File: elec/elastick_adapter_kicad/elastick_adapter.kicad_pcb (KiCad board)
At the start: 2 copper layers, 12 parts, among them J2 DE9_Pins_MountingHoles

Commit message: update kicad
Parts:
- removed R12, R13, R14, R16, R17, R25, R26, R27, R4: 330, Resistor_THT:R_Axial_DIN0207_L6.3mm_D2.5mm_P7.62mm_Horizontal
- added C1: 470µF, Capacitor_THT:CP_Radial_D8.0mm_P3.50mm, F.Cu at (101.3, 94.0)
- added C2: 100nF, Capacitor_THT:C_Disc_D5.0mm_W2.5mm_P5.00mm, F.Cu at (154.9, 93.9)
- added C3: 22nF, Capacitor_THT:C_Disc_D5.0mm_W2.5mm_P5.00mm, F.Cu at (97.8, 106.7)
- added C4: 22nF, Capacitor_THT:C_Disc_D5.0mm_W2.5mm_P5.00mm, F.Cu at (97.8, 115.6)
- added J2: USB-C Breakout, elastick:usbc, F.Cu at (139.0, 147.5)
- added SW1: POWER, Button_Switch_THT:SW_Slide_SPDT_Angled_CK_OS102011MA1Q, F.Cu at (106.1, 126.3)
- added SW2: ROTARY_SWITCH, Rotary_Encoder:RotaryEncoder_Alps_EC11E-Switch_Vertical_H20mm, B.Cu at (171.4, 124.5)
- DS1: renamed from U2; value ~ -> SSD1306 I2C OLED
- J1: renamed from J2; value DE9_Pins_MountingHoles -> DE-9JOYSTICK
- U1: value ~ -> LOLIN-D32
- moved DS1 72.9 mm to (127.7, 138.2), turned to 0 degrees
- moved U1 16.2 mm to (134.7, 134.8)
- moved J1 9.65 mm to (144.0, 48.6)
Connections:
- DS1 pad 1: unconnected-(U2-vcc-Pad1) -> Net-(DS1-vcc)
- DS1 pad 2: unconnected-(U2-gnd-Pad2) -> Net-(DS1-gnd)
- DS1 pad 3: unconnected-(U2-scl-Pad3) -> Net-(DS1-scl)
- DS1 pad 4: unconnected-(U2-sda-Pad4) -> Net-(DS1-sda)
- J1 pad 1: Net-(J2-Pad1) -> Net-(U1-4)
- J1 pad 2: Net-(J2-Pad2) -> Net-(U1-17)
- J1 pad 3: Net-(J2-Pad3) -> Net-(U1-26)
- J1 pad 4: Net-(J2-Pad4) -> Net-(U1-14)
- J1 pad 5: Net-(J2-Pad5) -> Net-(C4-Pad2)
- J1 pad 6: Net-(J2-Pad6) -> Net-(U1-16)
- J1 pad 7: Net-(J2-Pad7) -> Net-(U1-25)
- J1 pad 8: Net-(J2-Pad8) -> Net-(U1-27)
- J1 pad 9: Net-(J2-Pad9) -> Net-(C3-Pad2)
- U1 pad 1: unconnected-(U1-3v-Pad1) -> Net-(DS1-vcc)
- U1 pad 12: Net-(R12-Pad2) -> Net-(C3-Pad2)
- U1 pad 13: Net-(R13-Pad2) -> Net-(C4-Pad2)
- U1 pad 14: unconnected-(U1-enable-Pad14) -> Net-(SW1-B)
- U1 pad 17: unconnected-(U1-gnd-Pad17) -> Net-(DS1-gnd)
- U1 pad 21: unconnected-(U1-3-Pad21) -> Net-(DS1-sda)
- U1 pad 22: unconnected-(U1-21-Pad22) -> Net-(DS1-scl)
- U1 pad 32: unconnected-(U1-gnd-Pad32) -> Net-(DS1-gnd)
- U1 pad 5: unconnected-(U1-34-Pad5) -> Net-(U1-34)
- U1 pad 6: unconnected-(U1-32-Pad6) -> Net-(U1-32)
- U1 pad 7: unconnected-(U1-33-Pad7) -> Net-(U1-33)
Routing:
- net Net-(C4-Pad2): track 0.00 -> 122.2 mm
- net Net-(C3-Pad2): track 0.00 -> 116.2 mm
- net Net-(U1-27): track 0.00 -> 110.3 mm
- net Net-(U1-14): track 0.00 -> 109.7 mm
- net Net-(U1-26): track 0.00 -> 100.8 mm
- net Net-(U1-25): track 0.00 -> 100.0 mm
- net Net-(U1-4): track 0.00 -> 99.5 mm
- net Net-(U1-16): track 0.00 -> 98.7 mm
- net Net-(U1-17): track 0.00 -> 92.1 mm
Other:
- board text added: "ARNOKAID"
- board text added: "design by"

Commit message: update kicad
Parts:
- SW1: footprint Button_Switch_THT:SW_Slide_SPDT_Angled_CK_OS102011MA1Q -> elastick:SW_90degrees_3pins; moved to B.Cu
- moved C2 39.4 mm to (115.5, 94.1), turned to 180 degrees
- moved C1 28.5 mm to (114.3, 68.6), turned to 0 degrees
- moved J1 23.5 mm to (144.0, 72.1)
- moved C4 14.2 mm to (110.6, 109.2)
- moved C3 13.3 mm to (110.6, 102.9)
- moved SW2 11.4 mm to (160.0, 124.5)
- moved SW1 8.19 mm to (113.4, 130.0), turned to 90 degrees
- moved J2 3.08 mm to (135.9, 147.5)
- moved DS1 1.27 mm to (129.0, 138.2)
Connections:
- SW1 pad 1: Net-(DS1-gnd) -> unconnected-(SW1-A-Pad1)
- SW1 pad 2: Net-(SW1-B) -> Net-(DS1-gnd)
- SW1 pad 3: unconnected-(SW1-C-Pad3) -> Net-(SW1-C)
- SW2 pad A: Net-(U1-32) -> Net-(DS1-gnd)
- SW2 pad B: Net-(U1-34) -> Net-(U1-18)
- SW2 pad C: Net-(DS1-gnd) -> Net-(U1-19)
- SW2 pad S1: Net-(DS1-gnd) -> Net-(U1-5)
- SW2 pad S2: Net-(U1-33) -> Net-(DS1-gnd)
- U1 pad 14: Net-(SW1-B) -> Net-(SW1-C)
- U1 pad 19: unconnected-(U1-22-Pad19) -> Net-(DS1-scl)
- U1 pad 21: Net-(DS1-sda) -> unconnected-(U1-3-Pad21)
- U1 pad 22: Net-(DS1-scl) -> Net-(DS1-sda)
- U1 pad 23: unconnected-(U1-19-Pad23) -> Net-(U1-19)
- U1 pad 24: unconnected-(U1-18-Pad24) -> Net-(U1-18)
- U1 pad 25: unconnected-(U1-5-Pad25) -> Net-(U1-5)
- U1 pad 5: Net-(U1-34) -> unconnected-(U1-34-Pad5)
- U1 pad 6: Net-(U1-32) -> unconnected-(U1-32-Pad6)
- U1 pad 7: Net-(U1-33) -> unconnected-(U1-33-Pad7)
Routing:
- net Net-(DS1-gnd): track 0.00 -> 298.0 mm
- net Net-(DS1-vcc): track 0.00 -> 91.1 mm
- net Net-(DS1-scl): track 0.00 -> 47.1 mm
- net Net-(U1-27): track 110.3 -> 68.1 mm
- net Net-(U1-14): track 109.7 -> 68.9 mm
- net Net-(DS1-sda): track 0.00 -> 39.5 mm
- net Net-(U1-25): track 100.0 -> 60.7 mm
- net Net-(U1-26): track 100.8 -> 61.5 mm
- net Net-(U1-16): track 98.7 -> 65.1 mm
- net Net-(U1-4): track 99.5 -> 65.9 mm
- net Net-(U1-17): track 92.1 -> 58.5 mm
- net Net-(U1-19): track 0.00 -> 27.0 mm
- net Net-(U1-18): track 0.00 -> 27.0 mm
- net Net-(U1-5): track 0.00 -> 22.3 mm
- net Net-(C4-Pad2): track 122.2 -> 103.1 mm
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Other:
- board outline added: 55.9 x 99.1 mm

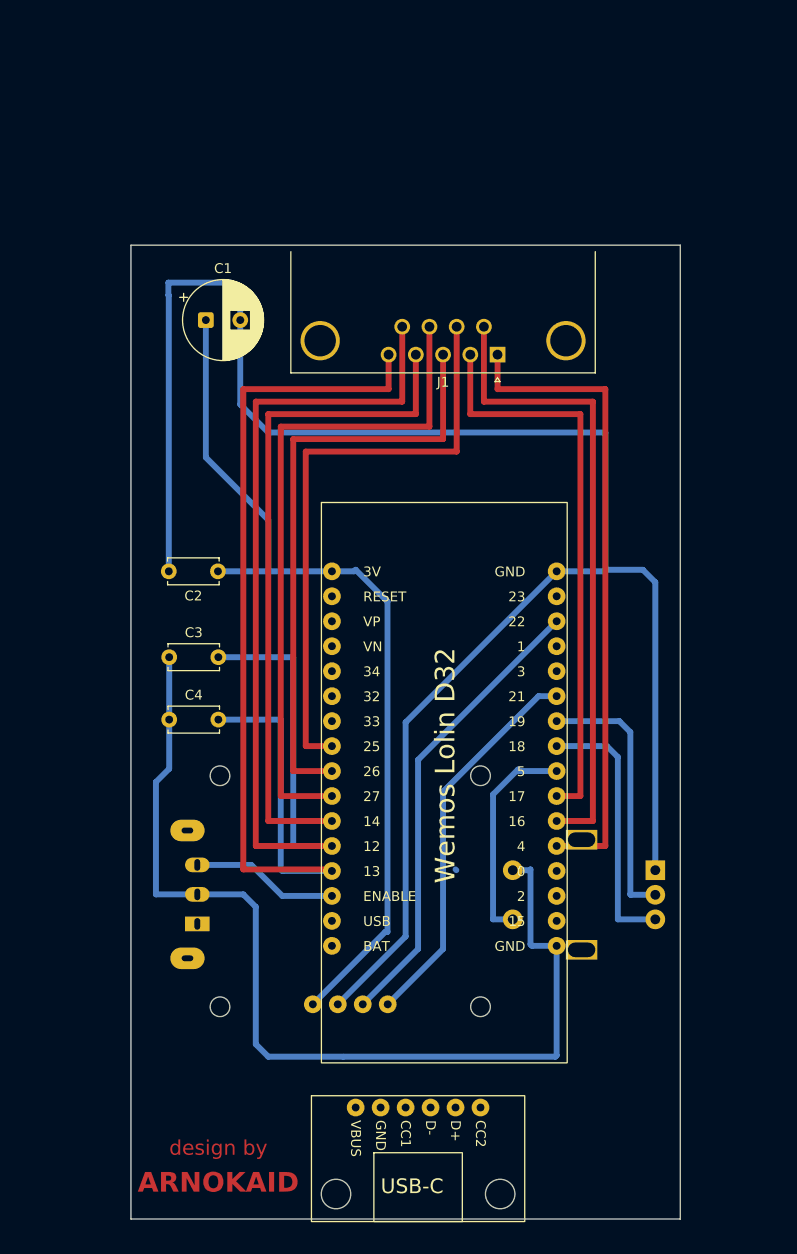
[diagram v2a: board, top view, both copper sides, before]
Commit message: update kicad with 3d for rotary button
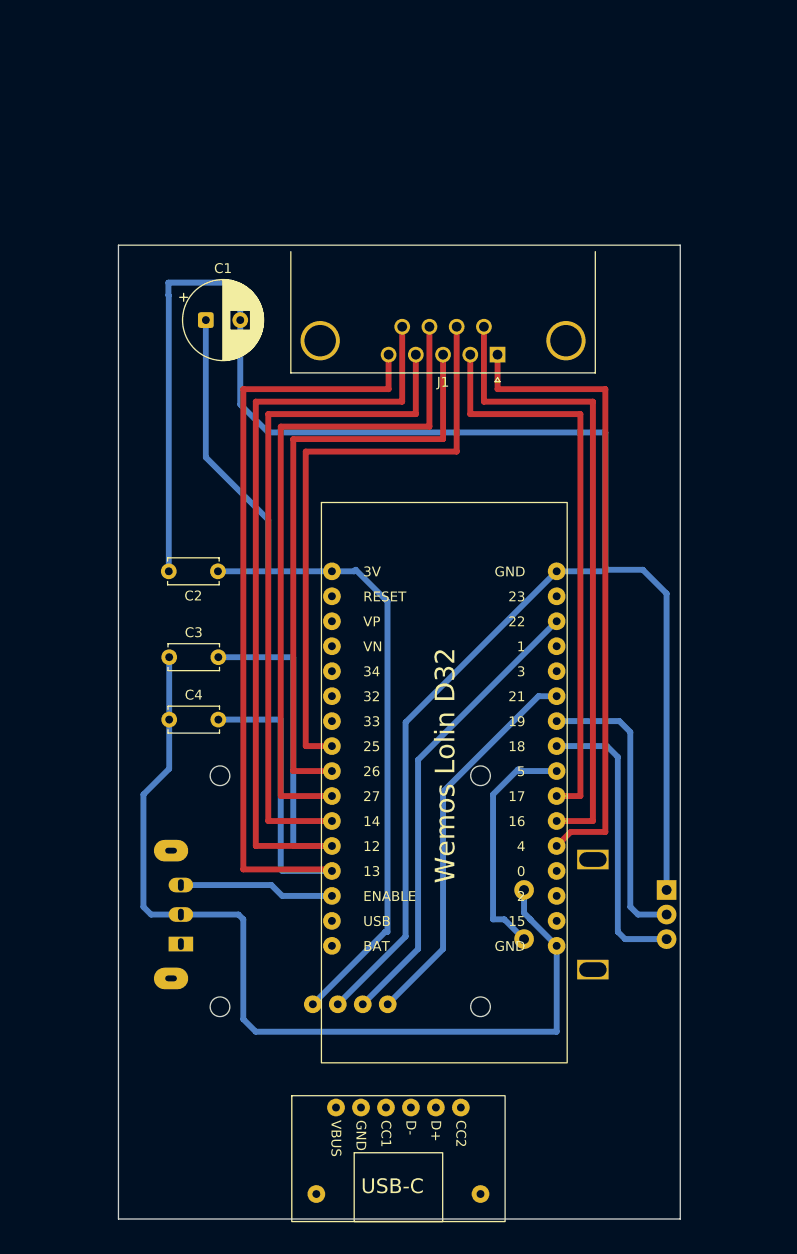
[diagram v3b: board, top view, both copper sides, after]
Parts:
- SW2: footprint Rotary_Encoder:RotaryEncoder_Alps_EC11E-Switch_Vertical_H20mm -> elastick:rotary_encoder
- moved SW1 2.64 mm to (111.8, 132.1)
- moved SW2 2.32 mm to (161.2, 126.5)
- moved J2 2.00 mm to (133.9, 147.5)
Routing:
- net Net-(DS1-gnd): track 298.0 -> 292.1 mm
- net Net-(U1-18): track 27.0 -> 29.7 mm
- net Net-(U1-19): track 27.0 -> 29.7 mm
- net Net-(U1-5): track 22.3 -> 24.3 mm
- net Net-(U1-4): track 65.9 -> 65.1 mm
- net Net-(SW1-C): track 15.2 -> 16.0 mm
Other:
- board size 55.9 x 99.1 mm -> 57.2 x 99.1 mm
- board text added: "Elastick Adapter v1.0.0"

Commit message: update kicad
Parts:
- moved C2 6.51 mm to (115.5, 87.6)
- moved C3 6.35 mm to (110.6, 96.5)
- moved C4 6.35 mm to (110.6, 102.9)
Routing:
- net Net-(U1-26): track 61.5 -> 55.6 mm
- net Net-(DS1-sda): track 39.5 -> 45.3 mm
- net Net-(U1-27): track 68.1 -> 63.0 mm
- net Net-(U1-14): track 68.9 -> 63.8 mm
- net Net-(DS1-scl): track 47.1 -> 51.0 mm
- net Net-(U1-5): track 24.3 -> 21.1 mm
- net Net-(DS1-gnd): track 292.1 -> 294.2 mm
- net Net-(C3-Pad2): track 106.1 -> 107.4 mm
- net Net-(C4-Pad2): track 103.1 -> 104.4 mm
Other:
- board size 57.2 x 99.1 mm -> 57.5 x 98.6 mm
- board text added: "Elastick Adapter 1.0.0"
- board text removed: "Elastick Adapter v1.0.0"

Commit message: update kicad
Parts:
- added REF**: battery_hole, elastick:battery_hole, F.Cu at (154.9, 105.4)
- added REF**: battery_hole, elastick:battery_hole, F.Cu at (116.8, 82.5)
- added REF**: battery_hole, elastick:battery_hole, F.Cu at (154.9, 82.5)
- added REF**: battery_hole, elastick:battery_hole, F.Cu at (116.8, 105.4)
- moved C4 3.62 mm to (108.0, 100.3)
- moved C3 3.62 mm to (108.0, 94.0)
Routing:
- net Net-(DS1-gnd): track 294.2 -> 309.0 mm
- net Net-(U1-16): track 65.1 -> 77.8 mm
- net Net-(U1-4): track 65.1 -> 77.8 mm
- net Net-(U1-17): track 58.5 -> 71.2 mm
- net Net-(DS1-vcc): track 91.4 -> 97.4 mm
- net Net-(C4-Pad2): track 104.4 -> 109.5 mm
- net Net-(C3-Pad2): track 107.4 -> 112.5 mm

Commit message: update kicad
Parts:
- added BAT_CABLE: battery_cable_hole, elastick:battery_cable_hole, F.Cu at (110.5, 144.1)
- added REF**: battery_hole, elastick:battery_hole, F.Cu at (165.7, 156.2)
- added REF**: battery_hole, elastick:battery_hole, F.Cu at (165.7, 66.0)
- added REF**: battery_hole, elastick:battery_hole, F.Cu at (109.2, 66.0)
- added REF**: battery_hole, elastick:battery_hole, F.Cu at (109.2, 156.2)
- moved J2 8.24 mm to (125.7, 148.6)
- moved SW2 6.83 mm to (168.0, 126.5)
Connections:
- net Net-(DS1-gnd) renamed /GND_NET
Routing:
- net /GND_NET: track 309.0 -> 316.8 mm
- net Net-(U1-19): track 29.7 -> 36.6 mm
- net Net-(U1-18): track 29.7 -> 36.6 mm
- net Net-(DS1-vcc): track 97.4 -> 93.1 mm
- net Net-(U1-5): track 21.1 -> 19.8 mm
- added copper zone on B.Cu, net /GND_NET
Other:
- board size 57.5 x 98.6 mm -> 64 x 100 mm
- board text added: "Greetings to: Acclaim Accolade Activision Bethesda Softworks Blue Byte Brøderbund Capcom Cinemaware Cobra Soft Codemasters Delphine Software Electronic Arts Elite Epyx ERE Informatique Exxos Hudson Soft Imagine Infogrames Irem Kalisto Konami Lankhor Loriciels Lucas Arts Microïds MicroProse Midway Mindscape Namco NovaLogic Ocean Psygnosis Rainbird Rainbow Arts SCi Sierra SNK subLOGIC Team 17 The B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"
- board text added: "Only Amiga makes it possible"
- board text added: "TO THE FUTURE"
- board text added: "TO THE PAST"
- board text added: "⇧"
